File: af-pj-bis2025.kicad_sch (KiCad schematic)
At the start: 110 parts, among them J1 Barrel_Jack_MountingPin, J10 Conn_01x02, J11 Conn_01x02, J12 FH28-10S-0.5SH_05_, J2 CN7, J3 Conn_Coaxial, J4 Conn_Coaxial, J5 CN10, J6 Conn_01x10, J7 Conn_01x06, J8 Conn_01x02, J9 Conn_01x02, SW1 PTS 647 SN50 SMTR2 LFS, SW2 PTS 647 SN50 SMTR2 LFS, U1 MIC5237-5.0YT, U2 ALD114904APAL, U3 OPA2380AIDGKR, U4 THS4552IPWR, U5 REF5050IDR, U7 UA78L06ACPK, U8 ADS1220IPW, U9 ADR130BUJZ-REEL7

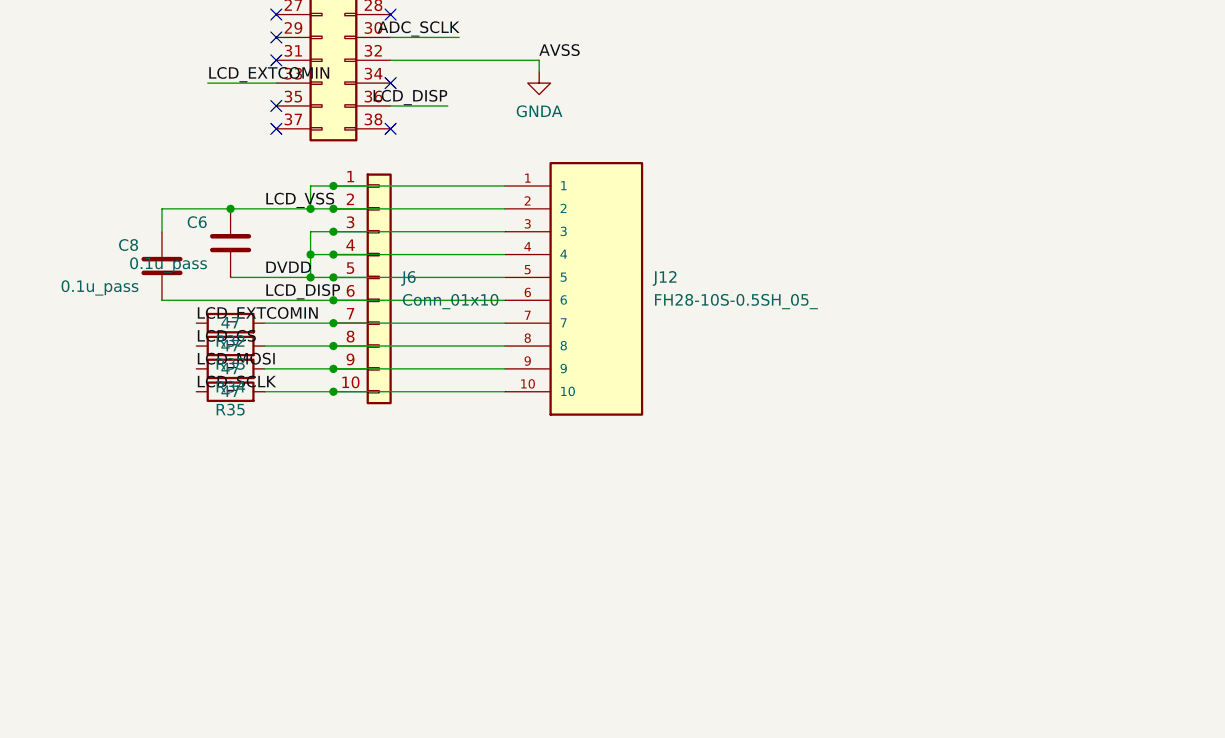
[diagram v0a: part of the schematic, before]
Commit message: LCDのコネクタ変更(schematic)
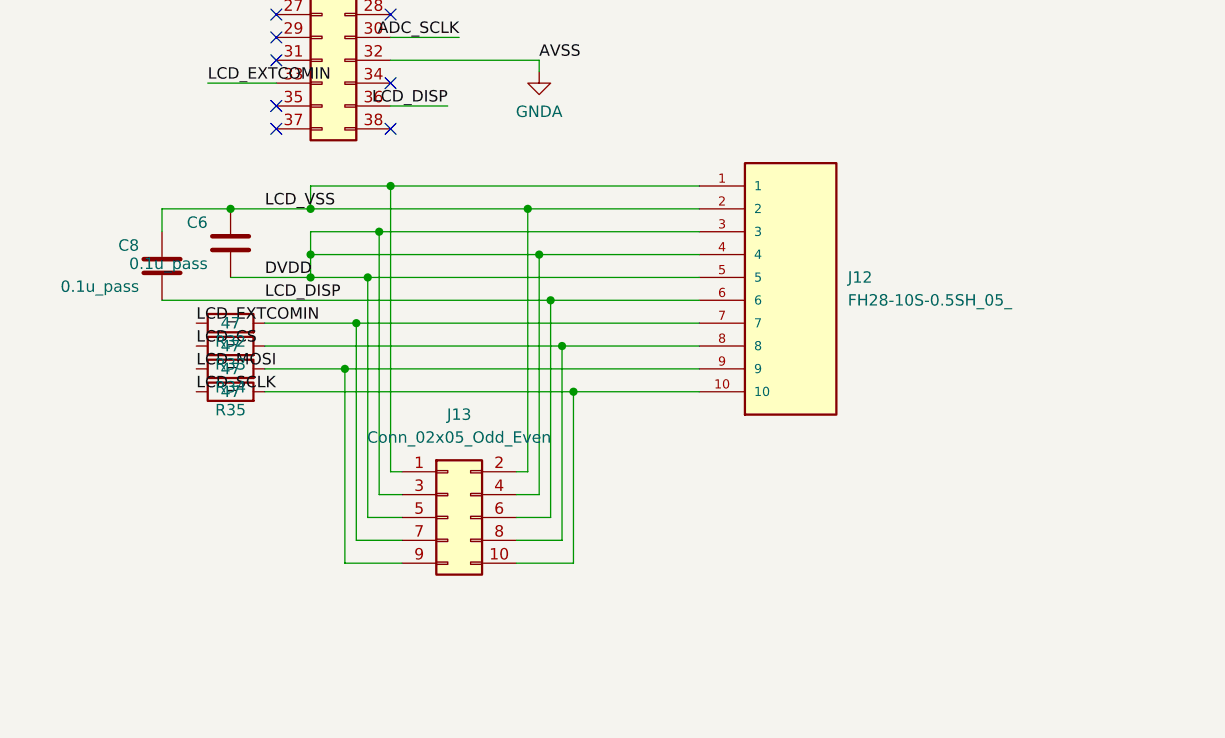
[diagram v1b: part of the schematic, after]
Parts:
- removed J6: Conn_01x10, Connector_JST:JST_XH_B10B-XH-A_1x10_P2.50mm_Vertical, symbol Connector_Generic:Conn_01x10
- added J13: Conn_02x05_Odd_Even, Connector_PinSocket_2.54mm:PinSocket_2x05_P2.54mm_Vertical, symbol Connector_Generic:Conn_02x05_Odd_Even
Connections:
- net +3V3: now also J13.3 (Pin_3), J13.4 (Pin_4), J13.5 (Pin_5)
- net GND: now also J13.1 (Pin_1), J13.2 (Pin_2)
- net LCD_DISP: now also J13.6 (Pin_6)
- net at J12.7, R32.2: now also J13.7 (Pin_7)
- net at J12.9, R34.2: now also J13.9 (Pin_9)
- net at J12.10, R35.2: now also J13.10 (Pin_10)
- net at J12.8, R33.2: now also J13.8 (Pin_8)
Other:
- moved on the sheet: J12

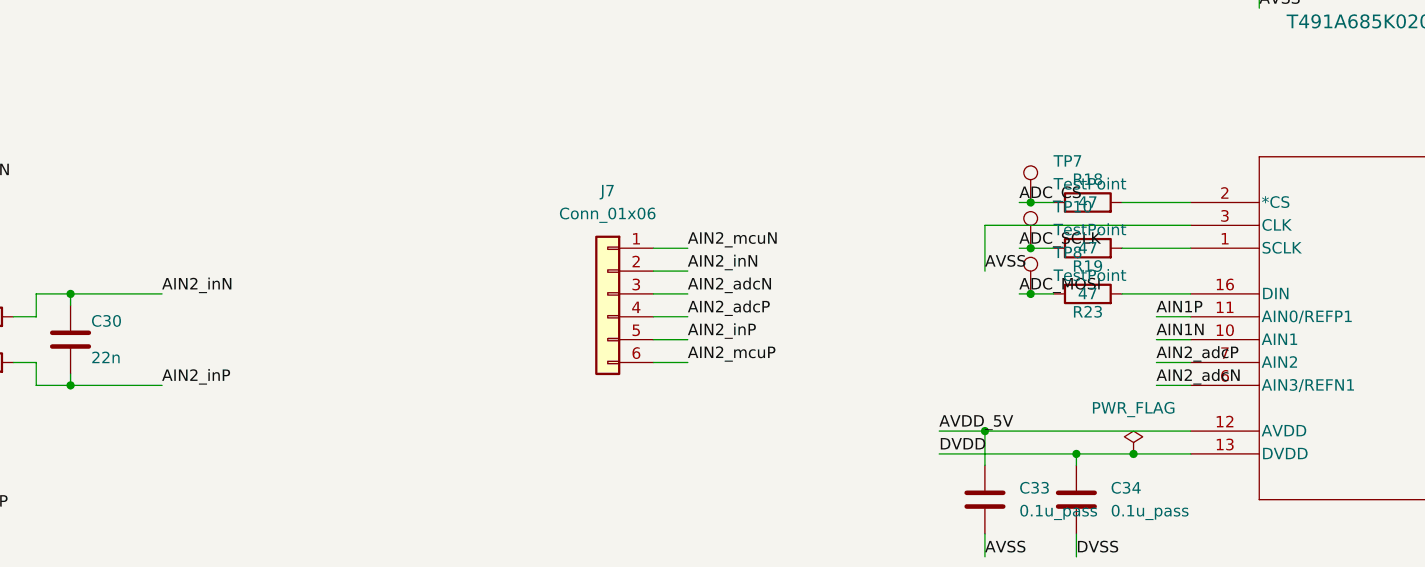
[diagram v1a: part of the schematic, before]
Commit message: ADCのコネクタ削除(Schematic)
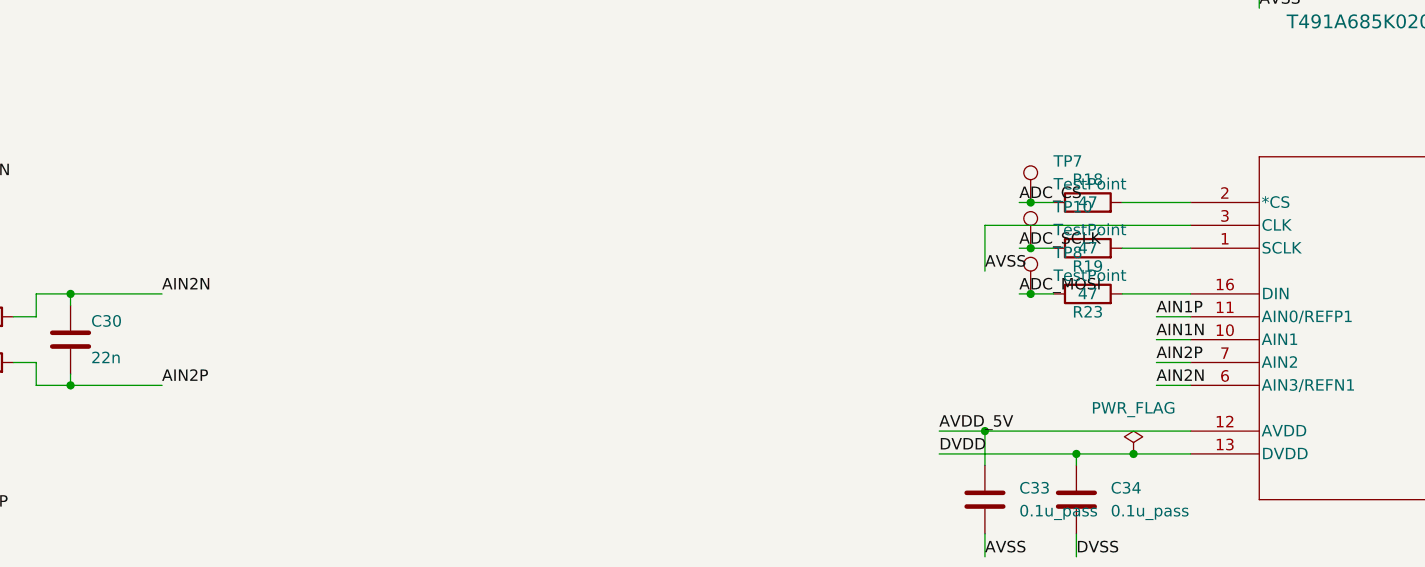
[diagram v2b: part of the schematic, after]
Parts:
- removed J7: Conn_01x06, Connector_PinHeader_2.54mm:PinHeader_1x06_P2.54mm_Vertical, symbol Connector_Generic:Conn_01x06
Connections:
- net AIN2_inN is gone; now on net AIN2N: C30.2, R26.2
- net AIN2_inP is gone; now on net AIN2P: C30.1, R28.2
- net AIN2_adcN renamed AIN2N
- net AIN2_adcP renamed AIN2P
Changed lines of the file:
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@@
 	(wire
 		(pts
-			(xy 241.3 331.47) (xy 245.11 331.47)
-		)
-		(stroke
-			(width 0)
-			(type default)
-		)
-	)
-	(wire
-		(pts
 			(xy 182.88 273.05) (xy 186.69 273.05)
 		)
@@
 	(wire
 		(pts
-			(xy 241.3 326.39) (xy 245.11 326.39)
-		)
-		(stroke
-			(width 0)
-			(type default)
-		)
-	)
-	(wire
-		(pts
 			(xy 165.1 137.16) (xy 173.99 137.16)
 		)
@@
 	(wire
 		(pts
-			(xy 241.3 318.77) (xy 245.11 318.77)
-		)
-		(stroke
-			(width 0)
-			(type default)
-		)
-	)
-	(wire
-		(pts
 			(xy 83.82 163.83) (xy 102.87 163.83)
 		)
@@
 	(wire
 		(pts
-			(xy 241.3 323.85) (xy 245.11 323.85)
-		)
-		(stroke
-			(width 0)
-			(type default)
-		)
-	)
-	(wire
-		(pts
 			(xy 229.87 140.97) (xy 231.14 140.97)
 		)
@@
 	(wire
 		(pts
-			(xy 241.3 321.31) (xy 245.11 321.31)
-		)
-		(stroke
-			(width 0)
-			(type default)
-		)
-	)
-	(wire
-		(pts
 			(xy 102.87 168.91) (xy 96.52 168.91)
 		)
@@
 	(wire
 		(pts
-			(xy 241.3 328.93) (xy 245.11 328.93)
-		)
-		(stroke
-			(width 0)
-			(type default)
-		)
-	)
-	(wire
-		(pts
 			(xy 356.87 86.36) (xy 356.87 83.82)
 		)
@@
 		)
 	)
-	(label "AIN2_inN"
+	(label "AIN2N"
 		(at 186.69 323.85 0)
 		(effects
@@
 		)
 	)
-	(label "AIN2_adcN"
+	(label "AIN2N"
 		(at 297.18 334.01 0)
 		(effects
@@
 		)
 	)
-	(label "AIN2_inP"
+	(label "AIN2P"
 		(at 186.69 334.01 0)
 		(effects
@@
 		)
 	)
-	(label "AIN2_inN"
-		(at 245.11 321.31 0)
-		(effects
-			(font
-				(size 1.27 1.27)
-			)
-			(justify left bottom)
-		)
-	)
 	(label "AVSS"
 		(at 220.98 196.85 0)
@@
 		)
 	)
-	(label "AIN2_mcuN"
-		(at 245.11 318.77 0)
-		(effects
-			(font
-				(size 1.27 1.27)
-			)
-			(justify left bottom)
-		)
-	)
 	(label "AIN1P"
 		(at 297.18 326.39 0)
@@
 		)
 	)
-	(label "AIN2_mcuP"
-		(at 245.11 331.47 0)
-		(effects
-			(font
-				(size 1.27 1.27)
-			)
-			(justify left bottom)
-		)
-	)
 	(label "AVSS"
 		(at 172.72 92.71 0)
@@
 		)
 	)
-	(label "AIN2_inP"
-		(at 245.11 328.93 0)
-		(effects
-			(font
-				(size 1.27 1.27)
-			)
-			(justify left bottom)
-		)
-	)
 	(label "DC_9V"
 		(at 247.65 275.59 0)
@@
 		)
 	)
-	(label "AIN2_adcN"
-		(at 245.11 323.85 0)
-		(effects
-			(font
-				(size 1.27 1.27)
-			)
-			(justify left bottom)
-		)
-	)
-	(label "AIN2_adcP"
+	(label "AIN2P"
 		(at 297.18 331.47 0)
 		(effects
@@
 		)
 	)
-	(label "AIN2_adcP"
-		(at 245.11 326.39 0)
-		(effects
-			(font
-				(size 1.27 1.27)
-			)
-			(justify left bottom)
-		)
-	)
 	(label "ADC_MOSI"
 		(at 361.95 104.14 0)
@@
 					(unit 1)
 				)
-			)
-		)
-	)
-	(symbol
-		(lib_id "Connector_Generic:Conn_01x06")
-		(at 236.22 323.85 0)
-		(mirror y)
-		(unit 1)
-		(exclude_from_sim no)
-		(in_bom yes)
-		(on_board yes)
-		(dnp no)
-		(fields_autoplaced yes)
-		(property "Reference" "J7"
-			(at 236.22 312.42 0)
-			(effects
-				(font
-					(size 1.27 1.27)
-				)
-			)
-		)
-		(property "Value" "Conn_01x06"
-			(at 236.22 314.96 0)
-			(effects
-				(font
-					(size 1.27 1.27)
-				)
-			)
-		)
-		(property "Footprint" "Connector_PinHeader_2.54mm:PinHeader_1x06_P2.54mm_Vertical"
-			(at 236.22 323.85 0)
-			(effects
-				(font
-					(size 1.27 1.27)
-				)
-				(hide yes)
-			)
-		)
-		(property "Datasheet" "~"
-			(at 236.22 323.85 0)
-			(effects
-				(font
-					(size 1.27 1.27)
-				)
-				(hide yes)
-			)
-		)
-		(property "Description" "Generic connector, single row, 01x06, script generated (kicad-library-utils/schlib/autogen/connector/)"
-			(at 236.22 323.85 0)
-			(effects
-				(font
-					(size 1.27 1.27)
-				)
-				(hide yes)
-			)
-		)
-		(pin "1"
-		)
-		(pin "2"
-		)
-		(pin "3"
-		)
-		(pin "5"
-		)
-		(pin "4"
-		)
-		(pin "6"
-		)
-		(instances
-			(project ""
-				(path "/0c43c024-04be-42a3-97bf-885833c3aea8"
-					(reference "J7")
-					(unit 1)
-				)

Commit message: アノテーションを再定義
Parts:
- renumbered C6 to C1, C7 to C10, C9 to C11, C10 to C12, C11 to C13, C12 to C14, C13 to C15, C14 to C16, C15 to C17, C16 to C18, C17 to C19, C8 to C2, C18 to C20, C23 to C21, C26 to C22, C27 to C23, C28 to C24, C29 to C25, C30 to C26, C31 to C27, C35 to C28, C19 to C29, C2 to C3, C20 to C30, C21 to C31, C22 to C32, C25 to C33, C32 to C34, C33 to C35, C34 to C36, C3 to C4, C1 to C5, C36 to C6, C37 to C7, C4 to C8, C5 to C9, J2 to J1, J5 to J2, J12 to J3, J13 to J4, J1 to J5, J3 to J6, J4 to J7, J9 to J8, J8 to J9, R37 to R1, R4 to R10, R5 to R11, R6 to R12, R7 to R13, R8 to R14, R9 to R15, R10 to R16, R11 to R17, R12 to R18, R13 to R19, R32 to R2, R14 to R20, R15 to R21, R16 to R22, R17 to R23, R21 to R24, R22 to R25, R25 to R26, R26 to R27, R27 to R28, R28 to R29, R33 to R3, R29 to R30, R30 to R31, R31 to R32, R18 to R33, R19 to R34, R20 to R35, R23 to R36, R24 to R37, R34 to R4, R35 to R5, R36 to R6, R1 to R7, R2 to R8, R3 to R9, TP5 to TP1, TP7 to TP10, TP10 to TP11, TP9 to TP12, TP8 to TP13, TP11 to TP14, TP13 to TP2, TP12 to TP3, TP1 to TP4, TP2 to TP5, TP3 to TP6, TP4 to TP7, TP14 to TP8, TP15 to TP9, U9 to U2, U2 to U3, U3 to U4, U4 to U5, U5 to U6
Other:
- moved on the sheet: C1, C10, C11, C12, C13, C14, C15, C16, C17, C18, C19, C2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

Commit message: 0.5Vrefのフットプリントを更新
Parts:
- U2: footprint UJ_6_ADI -> pj-bis2025:ADR130BUJZ_REEL7
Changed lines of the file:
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@@
 			)
 		)
-		(property "Footprint" "UJ_6_ADI"
+		(property "Footprint" "pj-bis2025:ADR130BUJZ_REEL7"
 			(at 110.49 106.68 0)
 			(effects

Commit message: アナログ配線完了
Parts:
- added TP15, TP16: TestPoint, Connector_Pin:Pin_D1.0mm_L10.0mm, symbol Connector:TestPoint
- C3: value C_Vin -> 22u
- C4: value 1µF -> 1u
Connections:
- net AIN1N: now also U8.6 (AIN3/REFN1); no longer U8.10 (AIN1)
- net AIN1P: now also U8.7 (AIN2); no longer U8.11 (AIN0/REFP1)
- net AIN2N: now also U8.10 (AIN1), TP15.1; no longer U8.6 (AIN3/REFN1)
- net AIN2P: now also U8.11 (AIN0/REFP1), TP16.1; no longer U8.7 (AIN2)
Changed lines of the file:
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@@
 	)
 	(junction
+		(at 198.12 339.09)
+		(diameter 0)
+		(color 0 0 0 0)
+	)
+	(junction
 		(at 113.03 71.12)
 		(diameter 0)
@@
 	)
 	(junction
+		(at 198.12 328.93)
+		(diameter 0)
+		(color 0 0 0 0)
+	)
+	(junction
 		(at 41.91 196.85)
 		(diameter 0)
@@
 	(wire
 		(pts
-			(xy 189.23 339.09) (xy 199.39 339.09)
+			(xy 189.23 339.09) (xy 198.12 339.09)
 		)
 		(stroke
@@
 	(wire
 		(pts
+			(xy 198.12 339.09) (xy 199.39 339.09)
+		)
+		(stroke
+			(width 0)
+			(type default)
+		)
+	)
+	(wire
+		(pts
 			(xy 107.95 309.88) (xy 107.95 328.93)
 		)
@@
 	(wire
 		(pts
-			(xy 189.23 328.93) (xy 199.39 328.93)
+			(xy 189.23 328.93) (xy 198.12 328.93)
 		)
 		(stroke
@@
 	(wire
 		(pts
+			(xy 198.12 328.93) (xy 199.39 328.93)
+		)
+		(stroke
+			(width 0)
+			(type default)
+		)
+	)
+	(wire
+		(pts
 			(xy 361.95 354.33) (xy 361.95 353.06)
 		)
@@
 		)
 	)
-	(label "AIN2N"
+	(label "AIN1N"
 		(at 370.84 345.44 0)
 		(effects
@@
 		)
 	)
-	(label "AIN1N"
+	(label "AIN2N"
 		(at 370.84 340.36 0)
 		(effects
@@
 		)
 	)
-	(label "AIN1P"
+	(label "AIN2P"
 		(at 370.84 337.82 0)
 		(effects
@@
 		)
 	)
-	(label "AIN2P"
+	(label "AIN1P"
 		(at 370.84 342.9 0)
 		(effects
@@
 			)
 		)
-		(property "Value" "1µF"
+		(property "Value" "1u"
 			(at 118.872 77.216 0)
 			(effects
@@
 			)
 		)
-		(property "Value" "C_Vin"
-			(at 98.552 80.772 0)
+		(property "Value" "22u"
+			(at 111.506 77.47 0)
 			(effects
 				(font
@@
 	(symbol
 		(lib_id "Connector:TestPoint")
+		(at 198.12 328.93 0)
+		(unit 1)
+		(exclude_from_sim no)
+		(in_bom yes)
+		(on_board yes)
+		(dnp no)
+		(fields_autoplaced yes)
+		(property "Reference" "TP15"
+			(at 200.66 324.3579 0)
+			(effects
+				(font
+					(size 1.27 1.27)
+				)
+				(justify left)
+			)
+		)
+		(property "Value" "TestPoint"
+			(at 200.66 326.8979 0)
+			(effects
+				(font
+					(size 1.27 1.27)
+				)
+				(justify left)
+			)
+		)
+		(property "Footprint" "Connector_Pin:Pin_D1.0mm_L10.0mm"
+			(at 203.2 328.93 0)
+			(effects
+				(font
+					(size 1.27 1.27)
+				)
+				(hide yes)
+			)
+		)
+		(property "Datasheet" "~"
+			(at 203.2 328.93 0)
+			(effects
+				(font
+					(size 1.27 1.27)
+				)
+				(hide yes)
+			)
+		)
+		(property "Description" "test point"
+			(at 198.12 328.93 0)
+			(effects
+				(font
+					(size 1.27 1.27)
+				)
+				(hide yes)
+			)
+		)
+		(pin "1"
+		)
+		(instances
+			(project "af-pj-bis2025"
+				(path "/0c43c024-04be-42a3-97bf-885833c3aea8"
+					(reference "TP15")
+					(unit 1)
+				)
+			)
+		)
+	)
+	(symbol
+		(lib_id "Connector:TestPoint")
 		(at 195.58 267.97 0)
 		(unit 1)
@@
 					(unit 1)
 				)
+			)
+		)
+	)
+	(symbol
+		(lib_id "Connector:TestPoint")
+		(at 198.12 339.09 0)
+		(unit 1)
+		(exclude_from_sim no)
+		(in_bom yes)
+		(on_board yes)
+		(dnp no)
+		(fields_autoplaced yes)
+		(property "Reference" "TP16"
+			(at 200.66 334.5179 0)
+			(effects
+				(font
+					(size 1.27 1.27)
+				)
+				(justify left)
+			)
+		)
+		(property "Value" "TestPoint"
+			(at 200.66 337.0579 0)
+			(effects
+				(font
+					(size 1.27 1.27)
+				)
+				(justify left)
+			)
+		)
+		(property "Footprint" "Connector_Pin:Pin_D1.0mm_L10.0mm"
+			(at 203.2 339.09 0)
+			(effects
+				(font
+					(size 1.27 1.27)
+				)
+				(hide yes)
+			)
+		)
+		(property "Datasheet" "~"
+			(at 203.2 339.09 0)
+			(effects
+				(font
+					(size 1.27 1.27)
+				)
+				(hide yes)
+			)
+		)
+		(property "Description" "test point"
+			(at 198.12 339.09 0)
+			(effects
+				(font
+					(size 1.27 1.27)
+				)
+				(hide yes)
+			)
+		)
+		(pin "1"
+		)
+		(instances
+			(project "af-pj-bis2025"
+				(path "/0c43c024-04be-42a3-97bf-885833c3aea8"
+					(reference "TP16")
+					(unit 1)
+				)

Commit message: GND以外終わり
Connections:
- net LCD_CS: now also J1.2 (Pin_2); no longer J2.17 (Pin_17)
- net LCD_DISP: now also J1.1 (Pin_1); no longer J2.36 (Pin_36)
- net LCD_EXTCOMIN: now also J1.3 (Pin_3); no longer J2.33 (Pin_33)
- net LCD_MOSI: now also J2.29 (Pin_29); no longer J2.15 (Pin_15)
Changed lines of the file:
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@@
 	)
 	(no_connect
-		(at 427.99 86.36)
-	)
-	(no_connect
 		(at 440.69 162.56)
 	)
@@
 	)
 	(no_connect
-		(at 427.99 185.42)
-	)
-	(no_connect
 		(at 440.69 180.34)
 	)
@@
 	)
 	(no_connect
-		(at 427.99 154.94)
+		(at 427.99 170.18)
 	)
 	(no_connect
-		(at 427.99 106.68)
+		(at 427.99 154.94)
 	)
 	(no_connect
-		(at 440.69 86.36)
+		(at 427.99 106.68)
 	)
 	(no_connect
@@
 	)
 	(no_connect
+		(at 427.99 167.64)
+	)
+	(no_connect
 		(at 443.23 91.44)
 	)
@@
 	)
 	(no_connect
+		(at 440.69 193.04)
+	)
+	(no_connect
 		(at 443.23 114.3)
 	)
@@
 	)
 	(no_connect
-		(at 427.99 88.9)
+		(at 427.99 190.5)
 	)
 	(no_connect
@@
 	(wire
 		(pts
-			(xy 420.37 162.56) (xy 427.99 162.56)
-		)
-		(stroke
-			(width 0)
-			(type default)
-		)
-	)
-	(wire
-		(pts
-			(xy 420.37 167.64) (xy 427.99 167.64)
-		)
-		(stroke
-			(width 0)
-			(type default)
-		)
-	)
-	(wire
-		(pts
 			(xy 189.23 337.82) (xy 189.23 339.09)
 		)
@@
 	(wire
 		(pts
+			(xy 420.37 162.56) (xy 427.99 162.56)
+		)
+		(stroke
+			(width 0)
+			(type default)
+		)
+	)
+	(wire
+		(pts
 			(xy 172.72 120.65) (xy 172.72 123.19)
 		)
@@
 	(wire
 		(pts
+			(xy 440.69 86.36) (xy 445.77 86.36)
+		)
+		(stroke
+			(width 0)
+			(type default)
+		)
+	)
+	(wire
+		(pts
 			(xy 52.07 199.39) (xy 114.3 199.39)
 		)
@@
 	(wire
 		(pts
-			(xy 447.04 193.04) (xy 440.69 193.04)
-		)
-		(stroke
-			(width 0)
-			(type default)
-		)
-	)
-	(wire
-		(pts
 			(xy 107.95 328.93) (xy 110.49 328.93)
 		)
@@
 	(wire
 		(pts
-			(xy 420.37 190.5) (xy 427.99 190.5)
-		)
-		(stroke
-			(width 0)
-			(type default)
-		)
-	)
-	(wire
-		(pts
 			(xy 143.51 248.92) (xy 107.95 248.92)
 		)
@@
 	(wire
 		(pts
+			(xy 422.91 88.9) (xy 427.99 88.9)
+		)
+		(stroke
+			(width 0)
+			(type default)
+		)
+	)
+	(wire
+		(pts
 			(xy 93.98 74.93) (xy 93.98 77.47)
 		)
@@
 	(wire
 		(pts
+			(xy 421.64 185.42) (xy 427.99 185.42)
+		)
+		(stroke
+			(width 0)
+			(type default)
+		)
+	)
+	(wire
+		(pts
 			(xy 374.65 327.66) (xy 351.79 327.66)
 		)
@@
 	(wire
 		(pts
+			(xy 422.91 86.36) (xy 427.99 86.36)
+		)
+		(stroke
+			(width 0)
+			(type default)
+		)
+	)
+	(wire
+		(pts
 			(xy 370.84 345.44) (xy 374.65 345.44)
 		)
@@
 	(wire
 		(pts
-			(xy 420.37 170.18) (xy 427.99 170.18)
-		)
-		(stroke
-			(width 0)
-			(type default)
-		)
-	)
-	(wire
-		(pts
 			(xy 147.32 260.35) (xy 147.32 261.62)
 		)
@@
 	)
 	(label "LCD_MOSI"
-		(at 420.37 167.64 0)
+		(at 421.64 185.42 0)
 		(effects
 			(font
@@
 	)
 	(label "LCD_EXTCOMIN"
-		(at 420.37 190.5 0)
+		(at 422.91 88.9 180)
 		(effects
 			(font
 				(size 1.27 1.27)
 			)
-			(justify left bottom)
+			(justify right bottom)
 		)
 	)
@@
 	)
 	(label "LCD_CS"
-		(at 420.37 170.18 0)
+		(at 445.77 86.36 0)
 		(effects
 			(font
@@
 	)
 	(label "LCD_DISP"
-		(at 447.04 193.04 180)
+		(at 422.91 86.36 180)
 		(effects
 			(font

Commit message: 基板完成
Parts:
- added TP17: TestPoint, Connector_Pin:Pin_D1.0mm_L10.0mm, symbol Connector:TestPoint
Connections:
- net VREF_0.5V: now also TP17.1
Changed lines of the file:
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@@
 	)
 	(junction
+		(at 177.8 111.76)
+		(diameter 0)
+		(color 0 0 0 0)
+	)
+	(junction
 		(at 361.95 353.06)
 		(diameter 0)
@@
 	(wire
 		(pts
-			(xy 172.72 111.76) (xy 180.34 111.76)
+			(xy 172.72 111.76) (xy 177.8 111.76)
 		)
 		(stroke
@@
 	(wire
 		(pts
+			(xy 177.8 111.76) (xy 180.34 111.76)
+		)
+		(stroke
+			(width 0)
+			(type default)
+		)
+	)
+	(wire
+		(pts
 			(xy 91.44 181.61) (xy 110.49 181.61)
 		)
@@
 					(unit 1)
 				)
+			)
+		)
+	)
+	(symbol
+		(lib_id "Connector:TestPoint")
+		(at 177.8 111.76 0)
+		(unit 1)
+		(exclude_from_sim no)
+		(in_bom yes)
+		(on_board yes)
+		(dnp no)
+		(fields_autoplaced yes)
+		(property "Reference" "TP17"
+			(at 180.34 107.1879 0)
+			(effects
+				(font
+					(size 1.27 1.27)
+				)
+				(justify left)
+			)
+		)
+		(property "Value" "TestPoint"
+			(at 180.34 109.7279 0)
+			(effects
+				(font
+					(size 1.27 1.27)
+				)
+				(justify left)
+			)
+		)
+		(property "Footprint" "Connector_Pin:Pin_D1.0mm_L10.0mm"
+			(at 182.88 111.76 0)
+			(effects
+				(font
+					(size 1.27 1.27)
+				)
+				(hide yes)
+			)
+		)
+		(property "Datasheet" "~"
+			(at 182.88 111.76 0)
+			(effects
+				(font
+					(size 1.27 1.27)
+				)
+				(hide yes)
+			)
+		)
+		(property "Description" "test point"
+			(at 177.8 111.76 0)
+			(effects
+				(font
+					(size 1.27 1.27)
+				)
+				(hide yes)
+			)
+		)
+		(pin "1"
+		)
+		(instances
+			(project "af-pj-bis2025"
+				(path "/0c43c024-04be-42a3-97bf-885833c3aea8"
+					(reference "TP17")
+					(unit 1)
+				)
